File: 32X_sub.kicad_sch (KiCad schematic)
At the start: 100 parts, among them IC511 315-5684, IC512 315-5788, IC515 74HC74, IC516 74LS00, T520 TestPoint, T526 TestPoint, T527 TestPoint, T528 TestPoint, T547 TestPoint, T548 TestPoint, T555 TestPoint, T599 AS, X501 *3

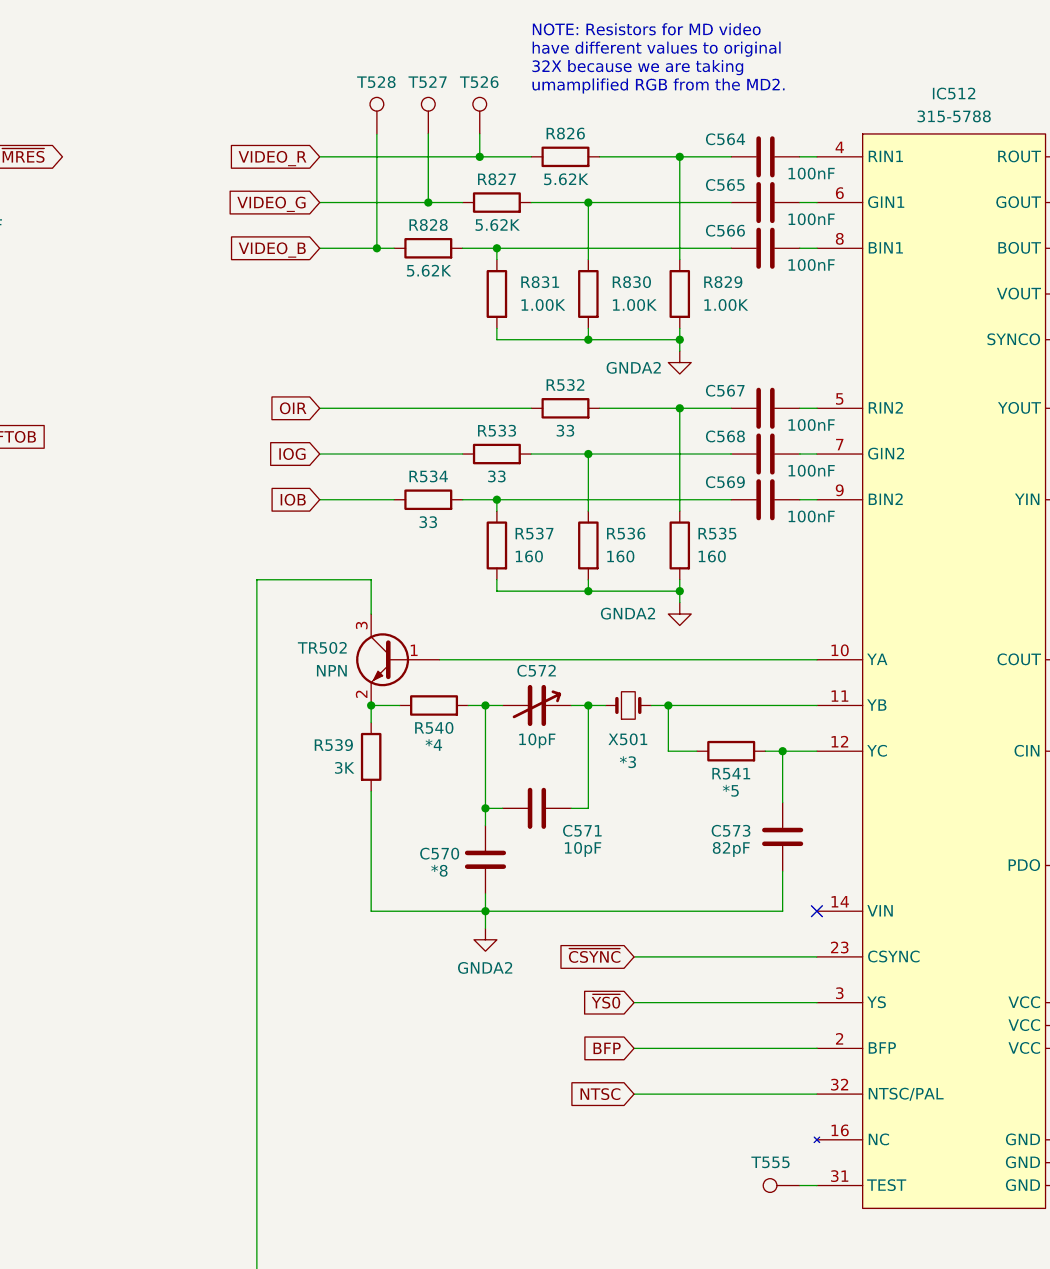
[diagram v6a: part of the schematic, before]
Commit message: Add RGB amp from 3BP.
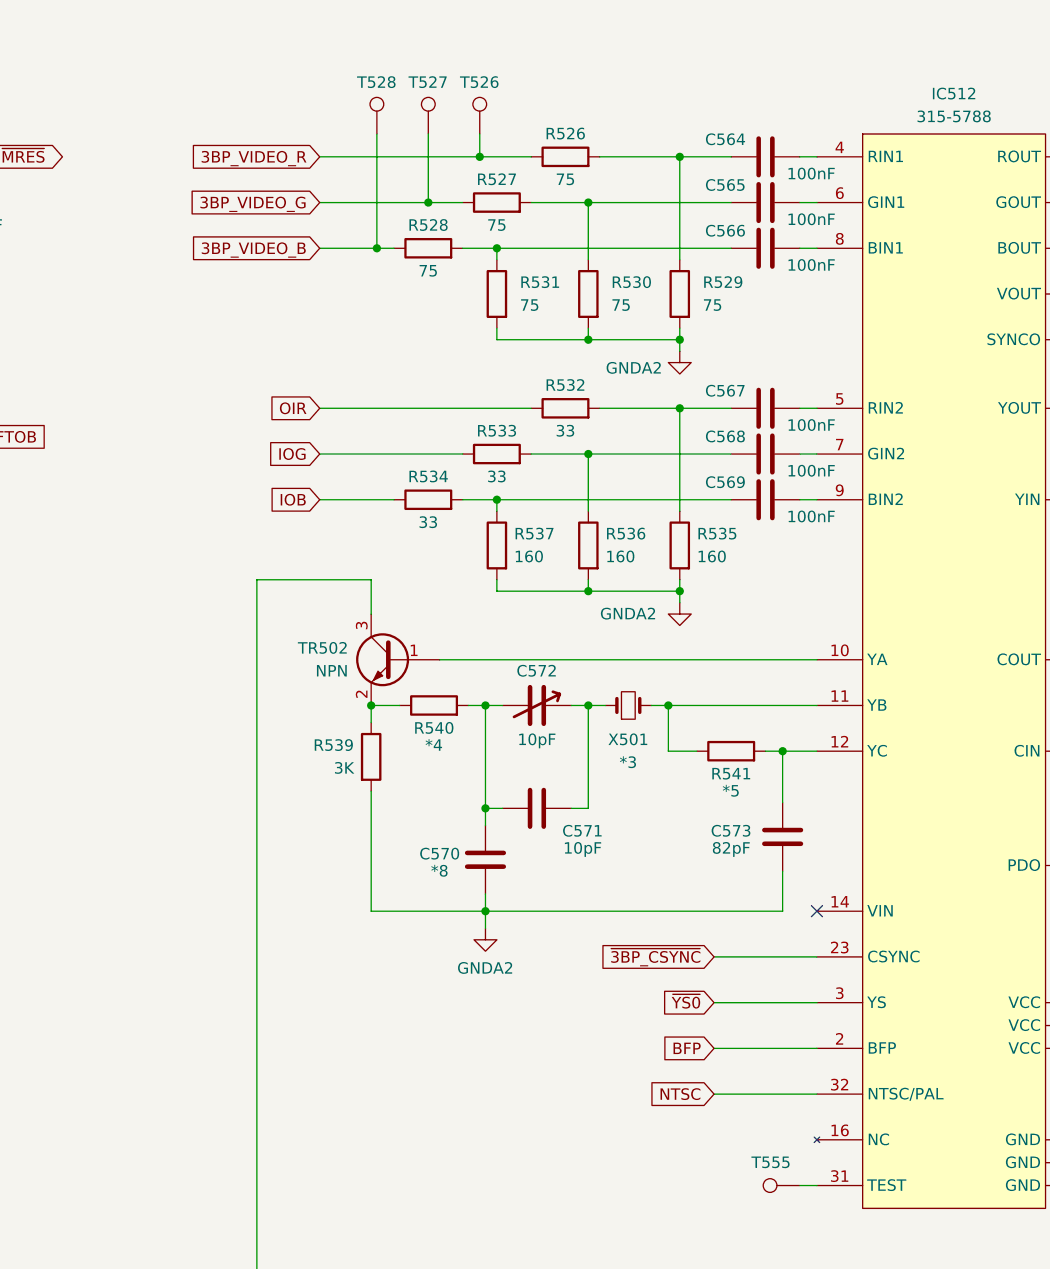
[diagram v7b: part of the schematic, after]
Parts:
- R526: renamed from R826; value 5.62K -> 75
- R527: renamed from R827; value 5.62K -> 75
- R528: renamed from R828; value 5.62K -> 75
- R529: renamed from R829; value 1.00K -> 75
- R530: renamed from R830; value 1.00K -> 75
- R531: renamed from R831; value 1.00K -> 75
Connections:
- net VIDEO_B renamed 3BP_VIDEO_B
- net VIDEO_G renamed 3BP_VIDEO_G
- net VIDEO_R renamed 3BP_VIDEO_R
- net ~{CSYNC} renamed ~{3BP_CSYNC}
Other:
- note removed: "NOTE: Resistors for MD video have different values to original 32X because we are taking umamplified RGB from the MD2."
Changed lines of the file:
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@@
     (stroke (width 0) (type default))
   )
-  (wire (pts (xy 275.59 121.92) (xy 295.91 121.92))
+  (wire (pts (xy 284.48 121.92) (xy 295.91 121.92))
     (stroke (width 0) (type default))
   )
@@
     (stroke (width 0) (type default))
   )
-  (wire (pts (xy 275.59 132.08) (xy 295.91 132.08))
+  (wire (pts (xy 284.48 132.08) (xy 295.91 132.08))
     (stroke (width 0) (type default))
   )
@@
     (stroke (width 0) (type default))
   )
-  (wire (pts (xy 275.59 127) (xy 295.91 127))
+  (wire (pts (xy 284.48 127) (xy 295.91 127))
     (stroke (width 0) (type default))
   )
@@
     (stroke (width 0) (type default))
   )
-  (wire (pts (xy 275.59 137.16) (xy 295.91 137.16))
+  (wire (pts (xy 284.48 137.16) (xy 295.91 137.16))
     (stroke (width 0) (type default))
   )
@@
     (effects (font (size 1.27 1.27) (thickness 0.254) bold) (justify left bottom))
   )
-  (text "NOTE: Resistors for MD video\nhave different values to original\n32X because we are taking\numamplified RGB from the MD2."
-    (at 264.16 26.035 0)
-    (effects (font (size 1.27 1.27)) (justify left bottom))
-  )
   (text "L504\nL505\nX501\nR540\nR541\nC570\nC574\nC575\nC578" (at 257.175 278.13 0)
     (effects (font (size 1.27 1.27)) (justify left bottom))
@@
     (effects (font (size 1.27 1.27)) (justify left bottom))
   )
-  (global_label "BFP" (shape input) (at 275.59 132.08 180) (fields_autoplaced)
+  (global_label "BFP" (shape input) (at 284.48 132.08 180) (fields_autoplaced)
     (effects (font (size 1.27 1.27)) (justify right))
-    (property "Intersheetrefs" "${INTERSHEET_REFS}" (at 268.9762 132.08 0)
+    (property "Intersheetrefs" "${INTERSHEET_REFS}" (at 277.8662 132.08 0)
       (effects (font (size 1.27 1.27)) (justify right) hide)
     )
@@
     )
   )
-  (global_label "VIDEO_R" (shape input) (at 240.665 33.02 180) (fields_autoplaced)
+  (global_label "~{3BP_CSYNC}" (shape input) (at 284.48 121.92 180) (fields_autoplaced)
+    (effects (font (size 1.27 1.27)) (justify right))
+    (property "Intersheetrefs" "${INTERSHEET_REFS}" (at 270.6091 121.92 0)
+      (effects (font (size 1.27 1.27)) (justify right) hide)
+    )
+  )
+  (global_label "3BP_VIDEO_R" (shape input) (at 240.665 33.02 180) (fields_autoplaced)
     (effects (font (size 1.27 1.27)) (justify right))
-    (property "Intersheetrefs" "${INTERSHEET_REFS}" (at 229.9993 33.02 0)
+    (property "Intersheetrefs" "${INTERSHEET_REFS}" (at 225.2822 33.02 0)
       (effects (font (size 1.27 1.27)) (justify right) hide)
     )
@@
     )
   )
-  (global_label "NTSC" (shape input) (at 275.59 137.16 180) (fields_autoplaced)
+  (global_label "NTSC" (shape input) (at 284.48 137.16 180) (fields_autoplaced)
     (effects (font (size 1.27 1.27)) (justify right))
-    (property "Intersheetrefs" "${INTERSHEET_REFS}" (at 267.8272 137.16 0)
+    (property "Intersheetrefs" "${INTERSHEET_REFS}" (at 276.7172 137.16 0)
       (effects (font (size 1.27 1.27)) (justify right) hide)
     )
@@
     )
   )
-  (global_label "~{YS0}" (shape input) (at 275.59 127 180) (fields_autoplaced)
+  (global_label "~{YS0}" (shape input) (at 284.48 127 180) (fields_autoplaced)
     (effects (font (size 1.27 1.27)) (justify right))
-    (property "Intersheetrefs" "${INTERSHEET_REFS}" (at 269.0972 127 0)
+    (property "Intersheetrefs" "${INTERSHEET_REFS}" (at 277.9872 127 0)
       (effects (font (size 1.27 1.27)) (justify right) hide)
     )
@@
     )
   )
-  (global_label "VIDEO_B" (shape input) (at 240.665 43.18 180) (fields_autoplaced)
+  (global_label "3BP_VIDEO_B" (shape input) (at 240.665 43.18 180) (fields_autoplaced)
     (effects (font (size 1.27 1.27)) (justify right))
-    (property "Intersheetrefs" "${INTERSHEET_REFS}" (at 229.9993 43.18 0)
+    (property "Intersheetrefs" "${INTERSHEET_REFS}" (at 225.2822 43.18 0)
       (effects (font (size 1.27 1.27)) (justify right) hide)
     )
   )
-  (global_label "VIDEO_G" (shape input) (at 240.665 38.1 180) (fields_autoplaced)
+  (global_label "3BP_VIDEO_G" (shape input) (at 240.665 38.1 180) (fields_autoplaced)
     (effects (font (size 1.27 1.27)) (justify right))
-    (property "Intersheetrefs" "${INTERSHEET_REFS}" (at 229.9993 38.1 0)
+    (property "Intersheetrefs" "${INTERSHEET_REFS}" (at 225.2822 38.1 0)
       (effects (font (size 1.27 1.27)) (justify right) hide)
     )
@@
     )
   )
-  (global_label "~{CSYNC}" (shape input) (at 275.59 121.92 180) (fields_autoplaced)
-    (effects (font (size 1.27 1.27)) (justify right))
-    (property "Intersheetrefs" "${INTERSHEET_REFS}" (at 266.4362 121.92 0)
-      (effects (font (size 1.27 1.27)) (justify right) hide)
-    )
-  )
   (global_label "XROUT" (shape output) (at 367.665 33.02 0) (fields_autoplaced)
     (effects (font (size 1.27 1.27)) (justify left))
@@
   (symbol (lib_id "Device:R") (at 267.97 33.02 90) (unit 1)
     (in_bom yes) (on_board yes) (dnp no)
-    (property "Reference" "R826" (at 267.97 30.48 90)
+    (property "Reference" "R526" (at 267.97 30.48 90)
       (effects (font (size 1.27 1.27)))
     )
-    (property "Value" "5.62K" (at 267.97 35.56 90)
+    (property "Value" "75" (at 267.97 35.56 90)
       (effects (font (size 1.27 1.27)))
     )
@@
       (project "Neptune"
         (path "/bcc23b51-b742-4ae5-9dd6-d96a24058944/edde10e2-ce08-4180-9fbe-ab298dfbfa4c"
-          (reference "R826") (unit 1)
+          (reference "R526") (unit 1)
         )
       )
@@
   (symbol (lib_id "Device:R") (at 260.35 38.1 90) (unit 1)
     (in_bom yes) (on_board yes) (dnp no)
-    (property "Reference" "R827" (at 260.35 35.56 90)
+    (property "Reference" "R527" (at 260.35 35.56 90)
       (effects (font (size 1.27 1.27)))
     )
-    (property "Value" "5.62K" (at 260.35 40.64 90)
+    (property "Value" "75" (at 260.35 40.64 90)
       (effects (font (size 1.27 1.27)))
     )
@@
       (project "Neptune"
         (path "/bcc23b51-b742-4ae5-9dd6-d96a24058944/edde10e2-ce08-4180-9fbe-ab298dfbfa4c"
-          (reference "R827") (unit 1)
+          (reference "R527") (unit 1)
         )
       )
@@
   (symbol (lib_id "Device:R") (at 260.35 48.26 0) (mirror y) (unit 1)
     (in_bom yes) (on_board yes) (dnp no) (fields_autoplaced)
-    (property "Reference" "R831" (at 262.89 46.99 0)
+    (property "Reference" "R531" (at 262.89 46.99 0)
       (effects (font (size 1.27 1.27)) (justify right))
     )
-    (property "Value" "1.00K" (at 262.89 49.53 0)
+    (property "Value" "75" (at 262.89 49.53 0)
       (effects (font (size 1.27 1.27)) (justify right))
     )
@@
       (project "Neptune"
         (path "/bcc23b51-b742-4ae5-9dd6-d96a24058944/edde10e2-ce08-4180-9fbe-ab298dfbfa4c"
-          (reference "R831") (unit 1)
+          (reference "R531") (unit 1)
         )
       )
@@
   (symbol (lib_id "Device:R") (at 252.73 43.18 90) (unit 1)
     (in_bom yes) (on_board yes) (dnp no)
-    (property "Reference" "R828" (at 252.73 40.64 90)
+    (property "Reference" "R528" (at 252.73 40.64 90)
       (effects (font (size 1.27 1.27)))
     )
-    (property "Value" "5.62K" (at 252.73 45.72 90)
+    (property "Value" "75" (at 252.73 45.72 90)
       (effects (font (size 1.27 1.27)))
     )
@@
       (project "Neptune"
         (path "/bcc23b51-b742-4ae5-9dd6-d96a24058944/edde10e2-ce08-4180-9fbe-ab298dfbfa4c"
-          (reference "R828") (unit 1)
+          (reference "R528") (unit 1)
         )
       )
@@
   (symbol (lib_id "Device:R") (at 280.67 48.26 0) (mirror y) (unit 1)
     (in_bom yes) (on_board yes) (dnp no) (fields_autoplaced)
-    (property "Reference" "R829" (at 283.21 46.99 0)
+    (property "Reference" "R529" (at 283.21 46.99 0)
       (effects (font (size 1.27 1.27)) (justify right))
     )
-    (property "Value" "1.00K" (at 283.21 49.53 0)
+    (property "Value" "75" (at 283.21 49.53 0)
       (effects (font (size 1.27 1.27)) (justify right))
     )
@@
       (project "Neptune"
         (path "/bcc23b51-b742-4ae5-9dd6-d96a24058944/edde10e2-ce08-4180-9fbe-ab298dfbfa4c"
-          (reference "R829") (unit 1)
+          (reference "R529") (unit 1)
         )
       )
@@
   (symbol (lib_id "Device:R") (at 270.51 48.26 0) (mirror y) (unit 1)
     (in_bom yes) (on_board yes) (dnp no) (fields_autoplaced)
-    (property "Reference" "R830" (at 273.05 46.99 0)
+    (property "Reference" "R530" (at 273.05 46.99 0)
       (effects (font (size 1.27 1.27)) (justify right))
     )
-    (property "Value" "1.00K" (at 273.05 49.53 0)
+    (property "Value" "75" (at 273.05 49.53 0)
       (effects (font (size 1.27 1.27)) (justify right))
     )
@@
       (project "Neptune"
         (path "/bcc23b51-b742-4ae5-9dd6-d96a24058944/edde10e2-ce08-4180-9fbe-ab298dfbfa4c"
-          (reference "R830") (unit 1)
+          (reference "R530") (unit 1)
         )
       )

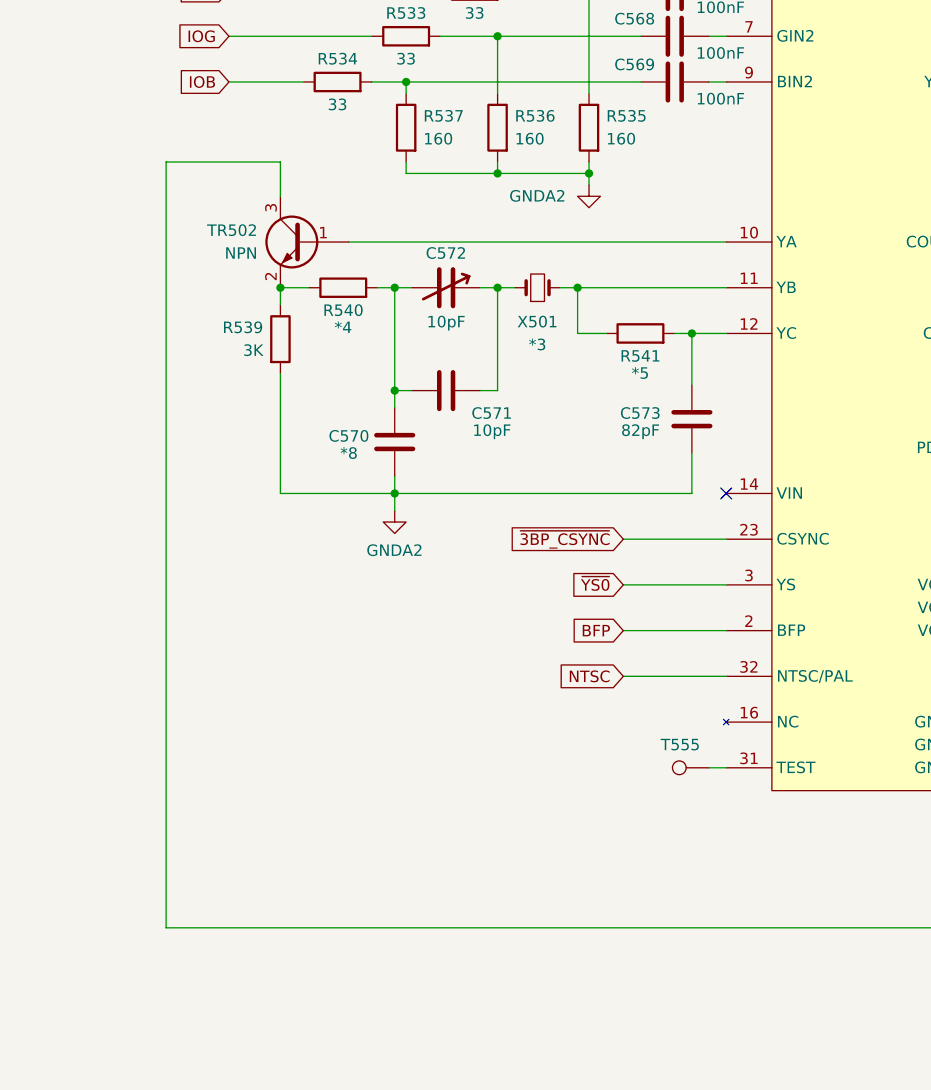
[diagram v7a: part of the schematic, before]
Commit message: Hook up SBCR (subcarrier) to 32X video encoder.
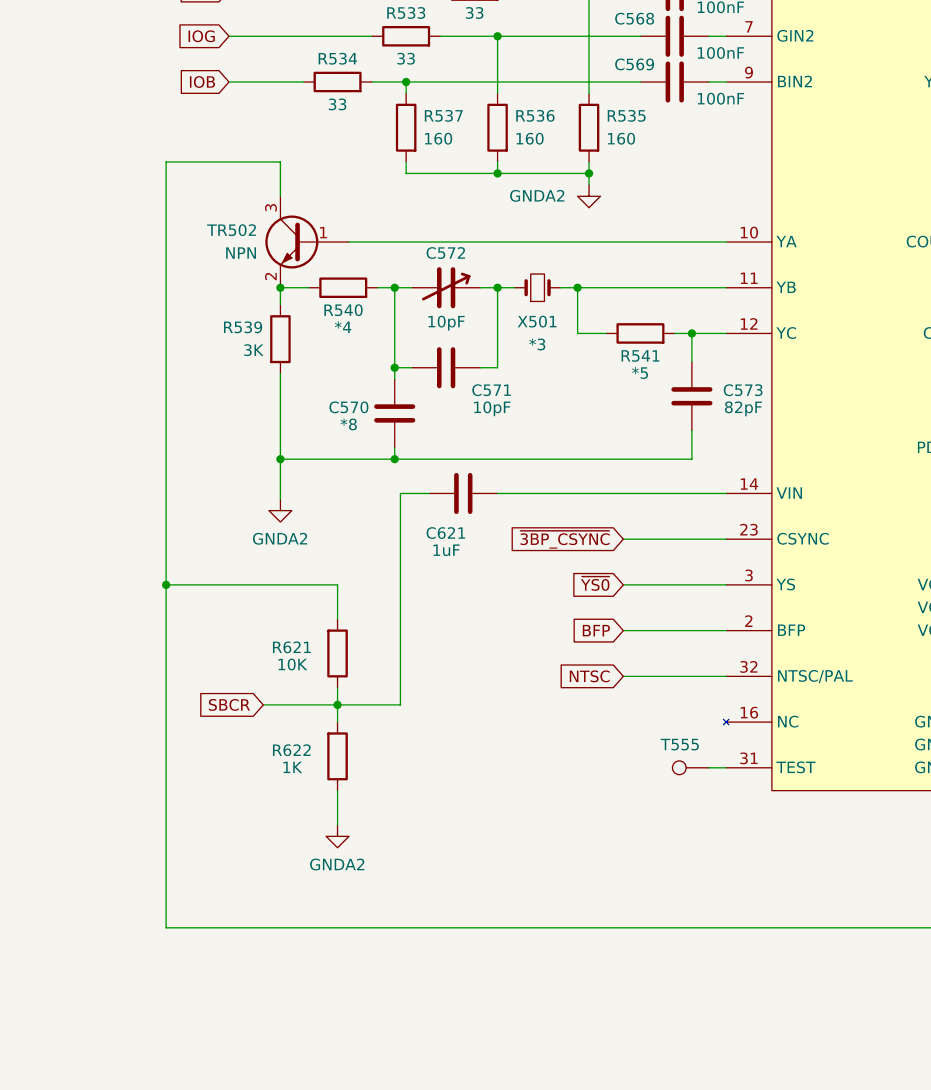
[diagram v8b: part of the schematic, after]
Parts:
- added C621: 1uF, Capacitor_SMD:C_0805_2012Metric, symbol Device:C
- added R621: 10K, Resistor_SMD:R_0805_2012Metric, symbol Device:R
- added R622: 1K, Resistor_SMD:R_0805_2012Metric, symbol Device:R
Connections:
- net GNDA2: now also R622.1
- net at C579.2, C580.2, CE17.1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: now also R621.2
- net at IC512.14 (VIN): now also C621.2
- new net SBCR: C621.1, R621.1, R622.2
- no-connect marks 10 -> 9
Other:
- moved on the sheet: C570, C571, C573
